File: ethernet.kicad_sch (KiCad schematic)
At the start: 33 parts, among them J4 RJ45_Amphenol_RJMG1BD3B8K1ANR, U21 KSZ8851-16MLL, U21B KSZ8851-16MLL, Y3 Crystal

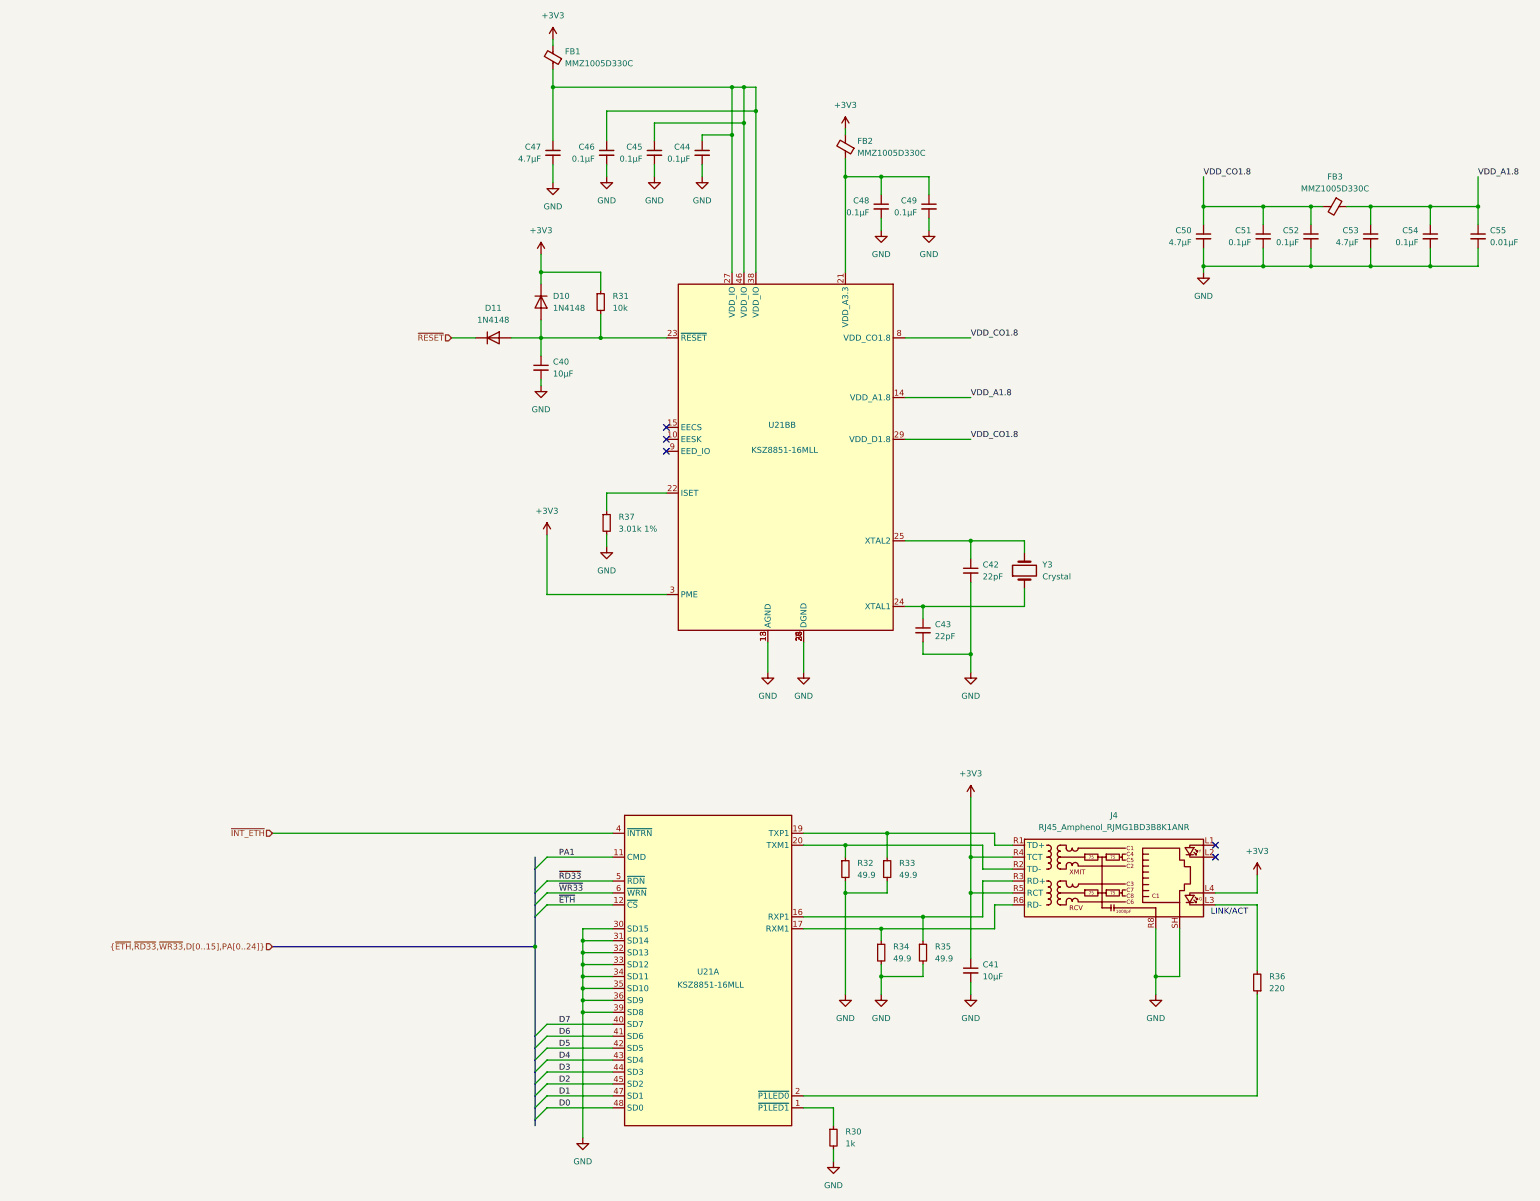
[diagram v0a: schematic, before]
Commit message: fix DRC errors, add RJ45 step model
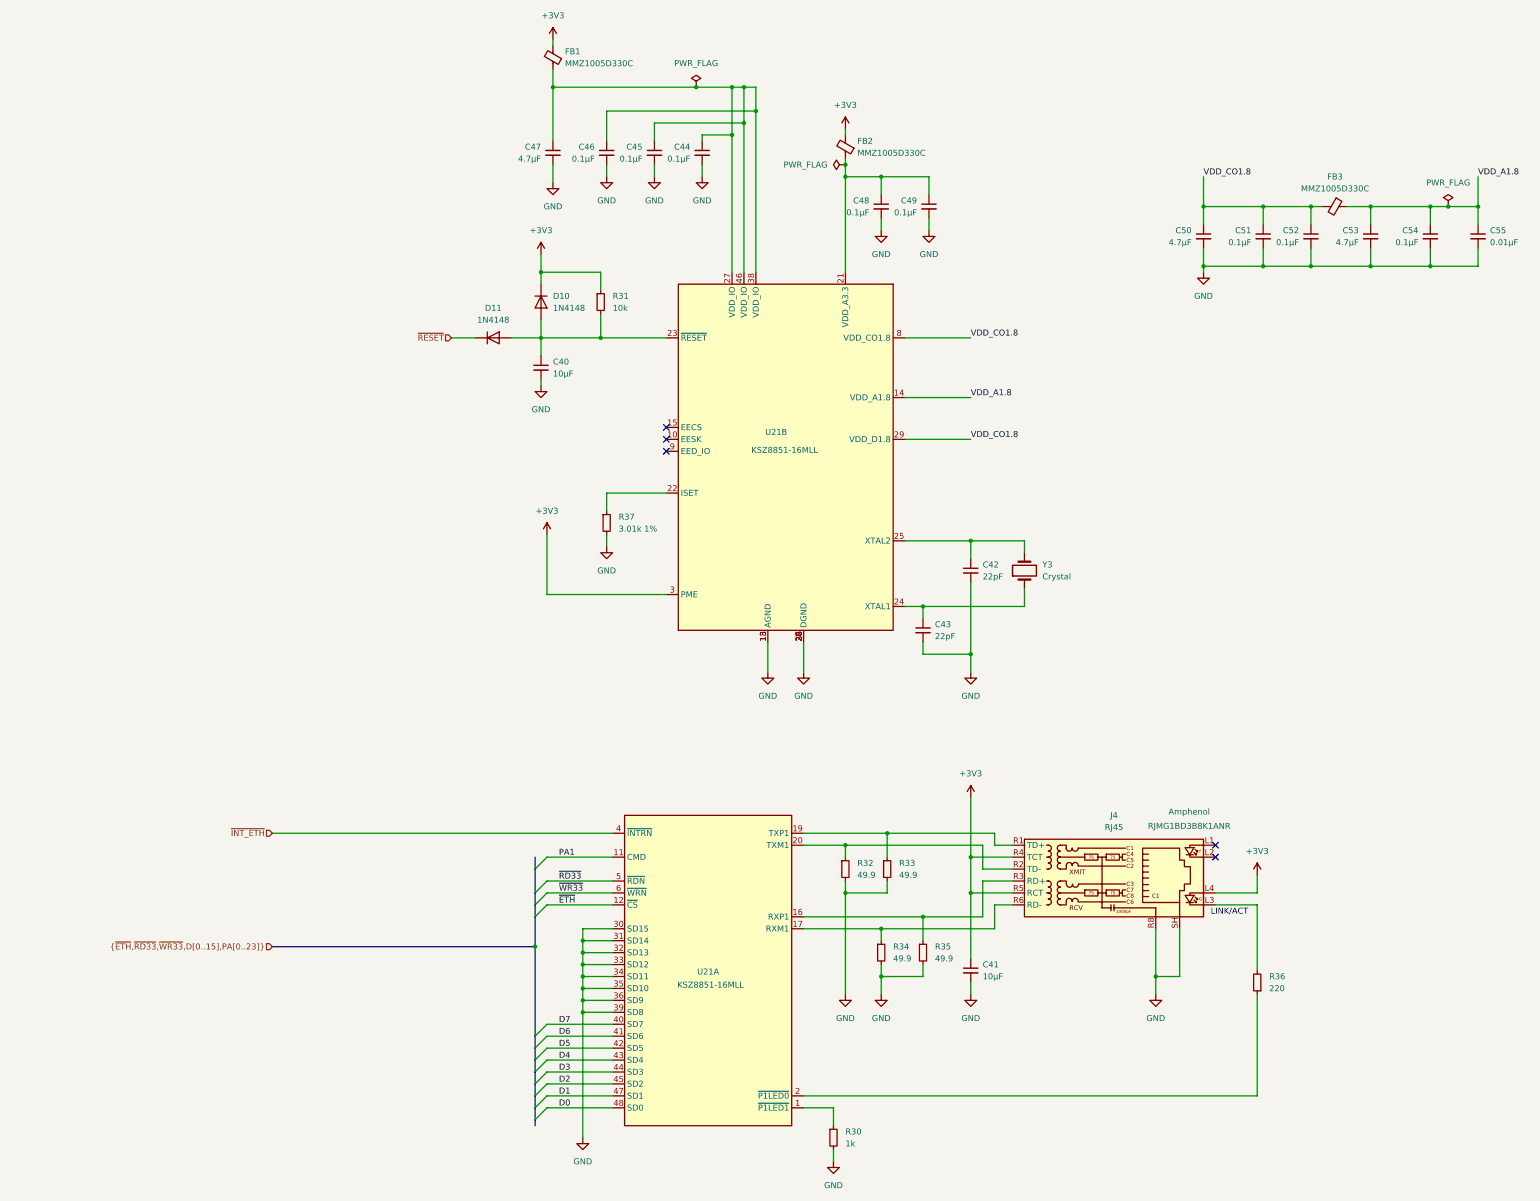
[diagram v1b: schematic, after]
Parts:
- J4: value RJ45_Amphenol_RJMG1BD3B8K1ANR -> RJ45; Mfg (none) -> Amphenol; Part (none) -> RJMG1BD3B8K1ANR
- renumbered U21B to U21

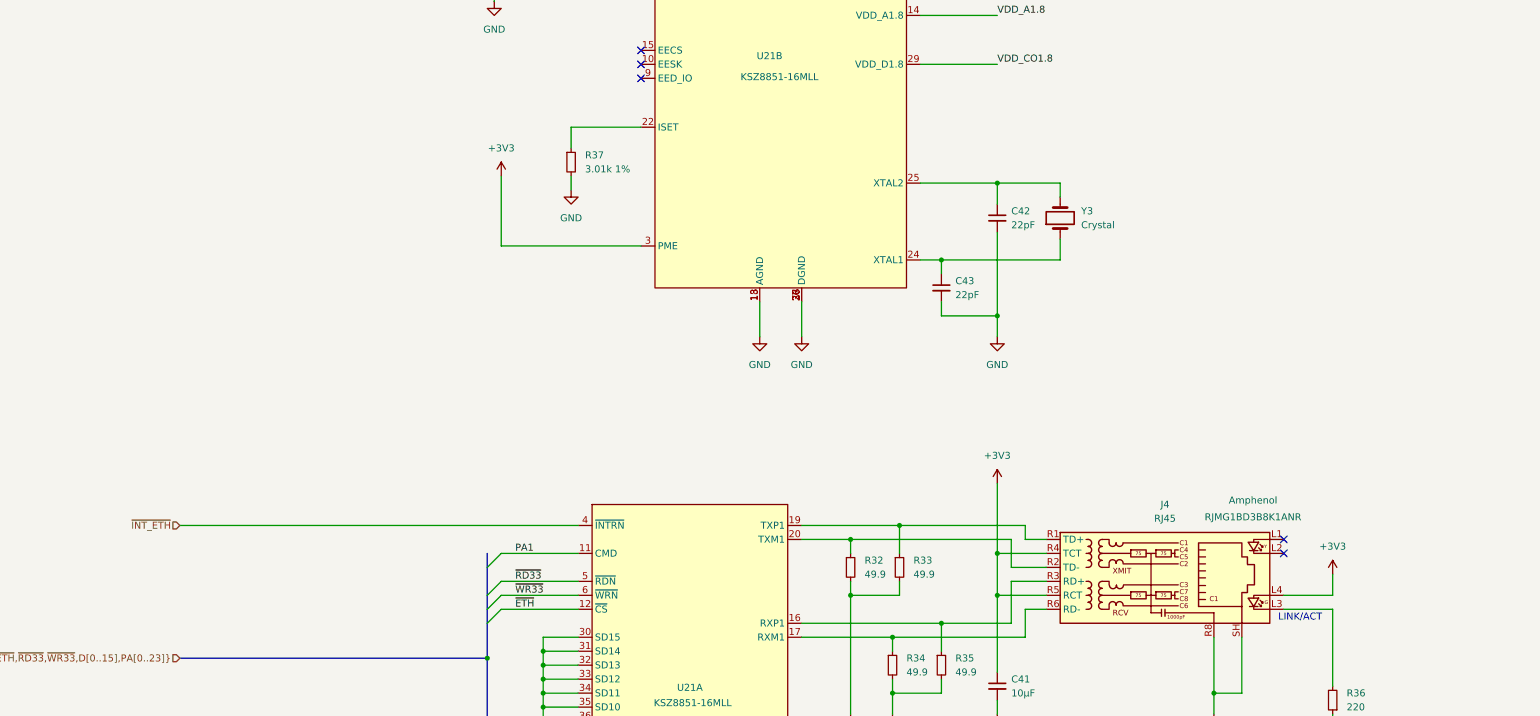
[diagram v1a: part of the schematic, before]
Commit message: route ethernet, reroute USB
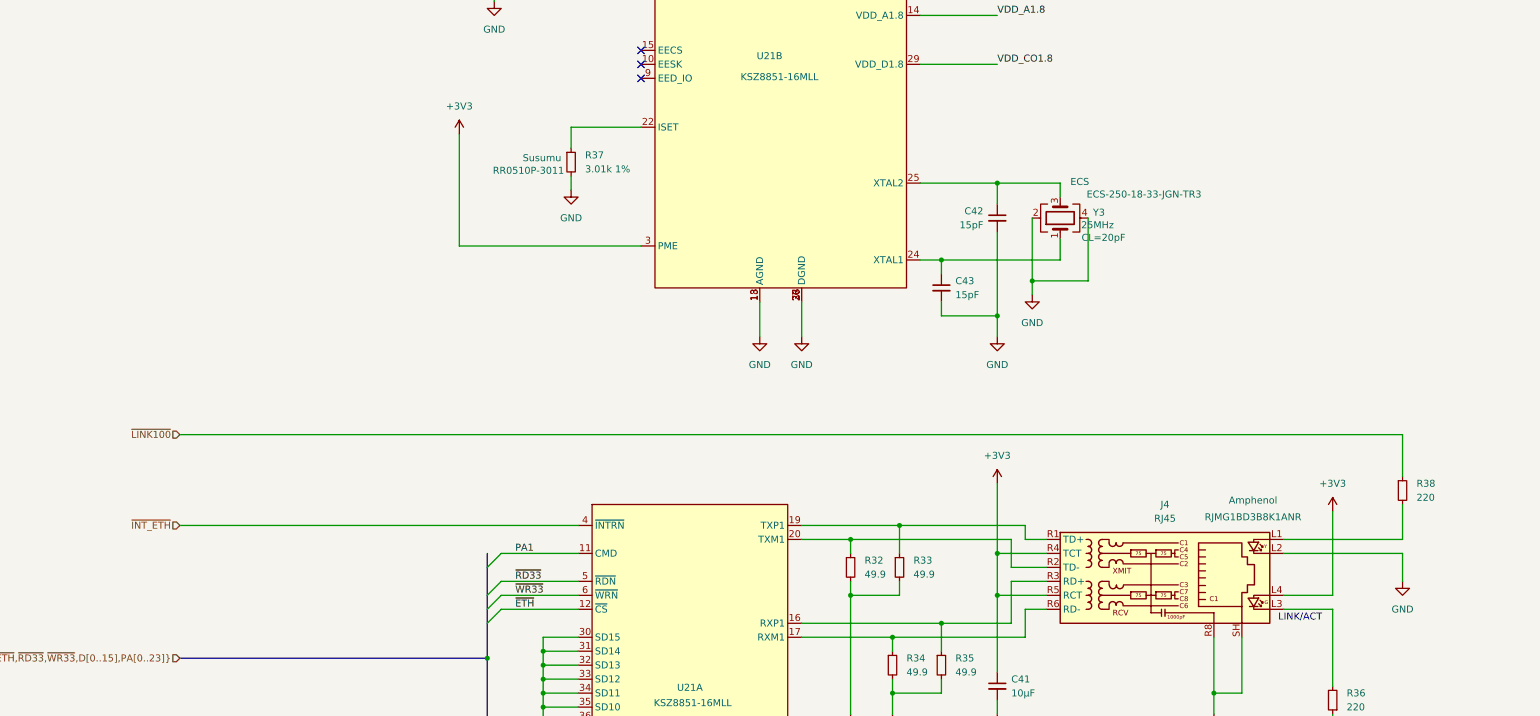
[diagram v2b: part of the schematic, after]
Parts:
- added R38: 220, Resistor_SMD:R_0402_1005Metric, symbol Device:R_Small
- C42, C43: value 22pF -> 15pF
- R37: footprint (none) -> Resistor_SMD:R_0402_1005Metric; Mfg (none) -> Susumu; Part (none) -> RR0510P-3011
- Y3: value Crystal -> 25MHz; footprint (none) -> Crystal:Crystal_SMD_3225-4Pin_3.2x2.5mm; symbol Device:Crystal -> Device:Crystal_GND24; Mfg (none) -> ECS; Param (none) -> CL=20pF; Part (none) -> ECS-250-18-33-JGN-TR3
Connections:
- net GND: now also J4.L2, Y3.2, Y3.4
- net at C42.1, U21.25 (XTAL2): now also Y3.3; no longer Y3.2
- net at J4.L1: now also R38.2
- new net ~{LINK100}: R38.1
- no-connect marks 5 -> 3

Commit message: correct datasheet, update 4148 footprint from 0805 to 0603
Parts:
- D10, D11: footprint Diode_SMD:D_0805_2012Metric -> Diode_SMD:D_0603_1608Metric
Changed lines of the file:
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@@
 			)
 		)
-		(property "Footprint" "Diode_SMD:D_0805_2012Metric"
+		(property "Footprint" "Diode_SMD:D_0603_1608Metric"
 			(at 101.6 88.9 0)
 			(effects
@@
 			)
 		)
-		(property "Footprint" "Diode_SMD:D_0805_2012Metric"
+		(property "Footprint" "Diode_SMD:D_0603_1608Metric"
 			(at 111.76 81.28 0)
 			(effects
